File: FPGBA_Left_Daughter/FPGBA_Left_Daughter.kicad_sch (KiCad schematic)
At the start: 8 parts

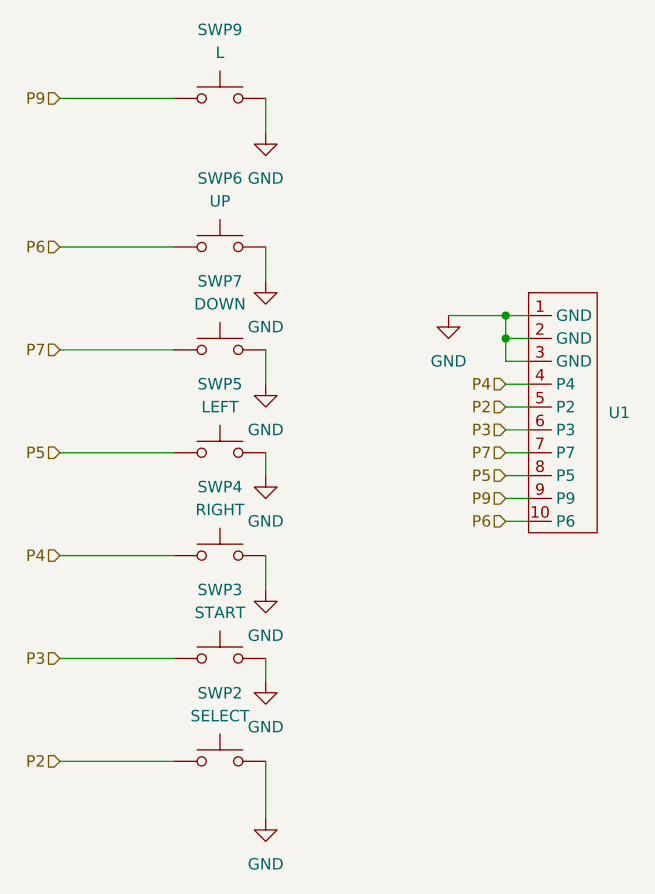
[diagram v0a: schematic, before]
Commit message: added JTAG + QSPI traces to PCB
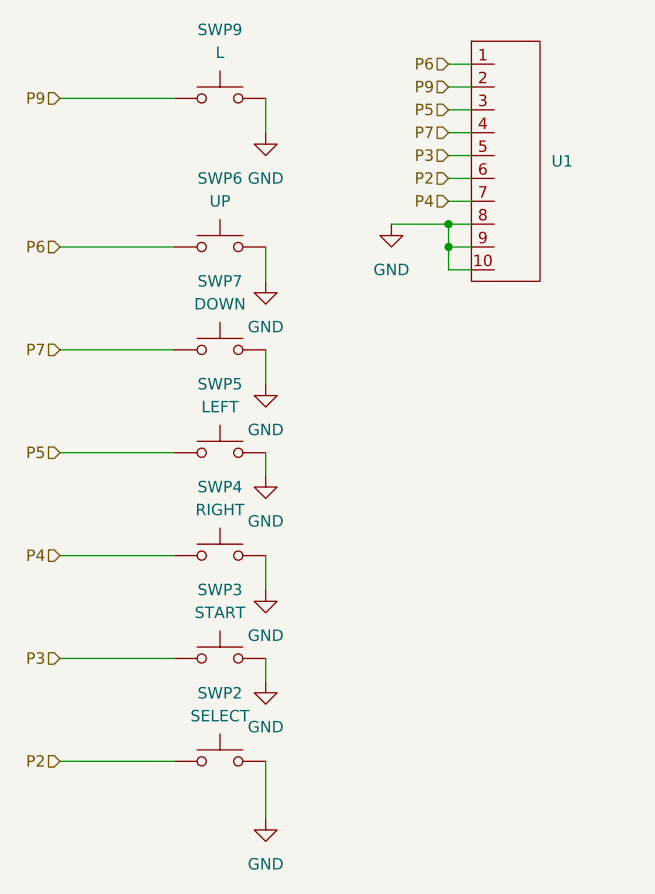
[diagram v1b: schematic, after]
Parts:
- U1: footprint Connector_FFC-FPC:Molex_54548-1071_1x10-1MP_P0.5mm_Horizontal -> Connector_FFC-FPC:Hirose_FH12-10S-0.5SH_1x10-1MP_P0.50mm_Horizontal
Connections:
- net GND: now also U1.10 (GND), U1.8 (GND), U1.9 (GND); no longer U1.1 (GND), U1.2 (GND), U1.3 (GND)
- net P2: now also U1.6 (P2); no longer U1.5 (P2)
- net P3: now also U1.5 (P3); no longer U1.6 (P3)
- net P4: now also U1.7 (P4); no longer U1.4 (P4)
- net P5: now also U1.3 (P5); no longer U1.8 (P5)
- net P6: now also U1.1 (P6); no longer U1.10 (P6)
- net P7: now also U1.4 (P7); no longer U1.7 (P7)
- net P9: now also U1.2 (P9); no longer U1.9 (P9)
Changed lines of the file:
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@@
 	(paper "A4")
 	(junction
-		(at 119.38 64.77)
+		(at 113.03 54.61)
 		(diameter 0)
 		(color 0 0 0 0)
 	)
 	(junction
-		(at 119.38 67.31)
+		(at 113.03 57.15)
 		(diameter 0)
 		(color 0 0 0 0)
@@
 	(wire
 		(pts
+			(xy 113.03 57.15) (xy 113.03 59.69)
+		)
+		(stroke
+			(width 0)
+			(type default)
+		)
+	)
+	(wire
+		(pts
 			(xy 92.71 57.15) (xy 92.71 60.96)
 		)
@@
 	(wire
 		(pts
-			(xy 119.38 69.85) (xy 121.92 69.85)
+			(xy 113.03 41.91) (xy 115.57 41.91)
 		)
 		(stroke
@@
 	(wire
 		(pts
-			(xy 119.38 72.39) (xy 121.92 72.39)
-		)
-		(stroke
-			(width 0)
-			(type default)
-		)
-	)
-	(wire
-		(pts
-			(xy 119.38 74.93) (xy 121.92 74.93)
-		)
-		(stroke
-			(width 0)
-			(type default)
-		)
-	)
-	(wire
-		(pts
-			(xy 119.38 64.77) (xy 121.92 64.77)
-		)
-		(stroke
-			(width 0)
-			(type default)
-		)
-	)
-	(wire
-		(pts
-			(xy 119.38 67.31) (xy 119.38 69.85)
+			(xy 113.03 44.45) (xy 115.57 44.45)
+		)
+		(stroke
+			(width 0)
+			(type default)
+		)
+	)
+	(wire
+		(pts
+			(xy 113.03 46.99) (xy 115.57 46.99)
+		)
+		(stroke
+			(width 0)
+			(type default)
+		)
+	)
+	(wire
+		(pts
+			(xy 113.03 36.83) (xy 115.57 36.83)
 		)
 		(stroke
@@
 	(wire
 		(pts
-			(xy 119.38 77.47) (xy 121.92 77.47)
-		)
-		(stroke
-			(width 0)
-			(type default)
-		)
-	)
-	(wire
-		(pts
-			(xy 113.03 64.77) (xy 119.38 64.77)
-		)
-		(stroke
-			(width 0)
-			(type default)
-		)
-	)
-	(wire
-		(pts
-			(xy 119.38 82.55) (xy 121.92 82.55)
+			(xy 113.03 49.53) (xy 115.57 49.53)
+		)
+		(stroke
+			(width 0)
+			(type default)
+		)
+	)
+	(wire
+		(pts
+			(xy 106.68 54.61) (xy 113.03 54.61)
+		)
+		(stroke
+			(width 0)
+			(type default)
+		)
+	)
+	(wire
+		(pts
+			(xy 113.03 54.61) (xy 115.57 54.61)
 		)
 		(stroke
@@
 	(wire
 		(pts
-			(xy 119.38 67.31) (xy 121.92 67.31)
+			(xy 113.03 39.37) (xy 115.57 39.37)
 		)
 		(stroke
@@
 	(wire
 		(pts
-			(xy 119.38 87.63) (xy 121.92 87.63)
-		)
-		(stroke
-			(width 0)
-			(type default)
-		)
-	)
-	(wire
-		(pts
-			(xy 119.38 64.77) (xy 119.38 67.31)
-		)
-		(stroke
-			(width 0)
-			(type default)
-		)
-	)
-	(wire
-		(pts
-			(xy 119.38 85.09) (xy 121.92 85.09)
+			(xy 113.03 59.69) (xy 115.57 59.69)
+		)
+		(stroke
+			(width 0)
+			(type default)
+		)
+	)
+	(wire
+		(pts
+			(xy 113.03 54.61) (xy 113.03 57.15)
+		)
+		(stroke
+			(width 0)
+			(type default)
+		)
+	)
+	(wire
+		(pts
+			(xy 113.03 57.15) (xy 115.57 57.15)
 		)
 		(stroke
@@
 	(wire
 		(pts
-			(xy 119.38 80.01) (xy 121.92 80.01)
+			(xy 113.03 52.07) (xy 115.57 52.07)
 		)
 		(stroke
@@
 	(hierarchical_label "P2"
 		(shape input)
-		(at 119.38 74.93 180)
+		(at 113.03 49.53 180)
 		(effects
 			(font
@@
 	(hierarchical_label "P6"
 		(shape input)
-		(at 119.38 87.63 180)
+		(at 113.03 36.83 180)
 		(effects
 			(font
@@
 	(hierarchical_label "P9"
 		(shape input)
-		(at 119.38 85.09 180)
+		(at 113.03 39.37 180)
 		(effects
 			(font
@@
 	(hierarchical_label "P4"
 		(shape input)
-		(at 119.38 72.39 180)
+		(at 113.03 52.07 180)
 		(effects
 			(font
@@
 	(hierarchical_label "P7"
 		(shape input)
-		(at 119.38 80.01 180)
+		(at 113.03 44.45 180)
 		(effects
 			(font
@@
 	(hierarchical_label "P5"
 		(shape input)
-		(at 119.38 82.55 180)
+		(at 113.03 41.91 180)
 		(effects
 			(font
@@
 	(hierarchical_label "P3"
 		(shape input)
-		(at 119.38 77.47 180)
+		(at 113.03 46.99 180)
 		(effects
 			(font
@@
 	(symbol
 		(lib_id "power:GND")
-		(at 113.03 64.77 0)
+		(at 106.68 54.61 0)
 		(unit 1)
 		(body_style 1)
@@
 		(fields_autoplaced yes)
 		(property "Reference" "#PWR08"
-			(at 113.03 71.12 0)
+			(at 106.68 60.96 0)
 			(hide yes)
 			(show_name no)
@@
 		)
 		(property "Value" "GND"
-			(at 113.03 69.85 0)
+			(at 106.68 59.69 0)
 			(show_name no)
 			(do_not_autoplace no)
@@
 		)
 		(property "Footprint" ""
-			(at 113.03 64.77 0)
+			(at 106.68 54.61 0)
 			(hide yes)
 			(show_name no)
@@
 		)
 		(property "Datasheet" ""
-			(at 113.03 64.77 0)
+			(at 106.68 54.61 0)
 			(hide yes)
 			(show_name no)
@@
 		)
 		(property "Description" "Power symbol creates a global label with name \"GND\" , ground"
-			(at 113.03 64.77 0)
+			(at 106.68 54.61 0)
 			(hide yes)
 			(show_name no)
@@
 	)
 	(symbol
+		(lib_name "FFC_Connector_10pin_1")
 		(lib_id "symbol_library:FFC_Connector_10pin")
-		(at 125.73 73.66 0)
+		(at 119.38 45.72 0)
 		(unit 1)
 		(body_style 1)
@@
 		(fields_autoplaced yes)
 		(property "Reference" "U1"
-			(at 130.81 75.5649 0)
+			(at 124.46 47.6249 0)
 			(show_name no)
 			(do_not_autoplace no)
@@
 		)
 		(property "Value" ""
-			(at 125.73 73.66 0)
-			(show_name no)
-			(do_not_autoplace no)
-			(effects
-				(font
-					(size 1.27 1.27)
-				)
-			)
-		)
-		(property "Footprint" "Connector_FFC-FPC:Molex_54548-1071_1x10-1MP_P0.5mm_Horizontal"
-			(at 125.73 73.66 0)
+			(at 119.38 45.72 0)
+			(show_name no)
+			(do_not_autoplace no)
+			(effects
+				(font
+					(size 1.27 1.27)
+				)
+			)
+		)
+		(property "Footprint" "Connector_FFC-FPC:Hirose_FH12-10S-0.5SH_1x10-1MP_P0.50mm_Horizontal"
+			(at 119.38 45.72 0)
 			(hide yes)
 			(show_name no)
@@
 		)
 		(property "Datasheet" ""
-			(at 125.73 73.66 0)
+			(at 119.38 45.72 0)
 			(hide yes)
 			(show_name no)
@@
 		)
 		(property "Description" ""
-			(at 125.73 73.66 0)
-			(hide yes)
-			(show_name no)
+			(at 119.38 45.72 0)
+			(hide yes)
+			(show_name no)
